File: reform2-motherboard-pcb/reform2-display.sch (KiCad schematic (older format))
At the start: 40 parts, among them J24 EDP_HEADER, U10 SN65DSI86IPAPQ1

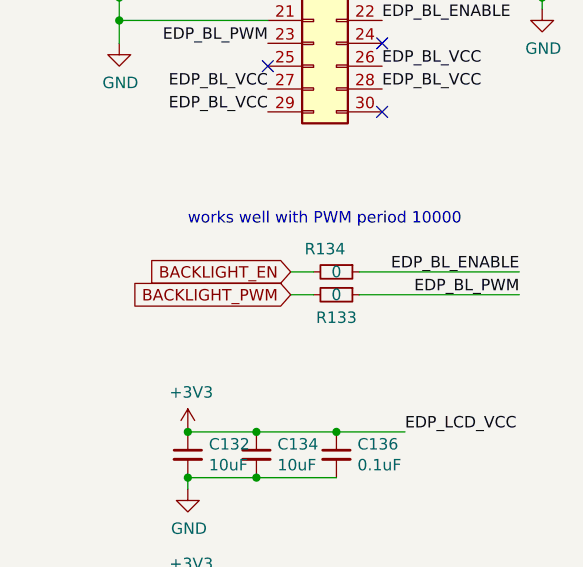
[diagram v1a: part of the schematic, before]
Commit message: reform2-motherboard: version D-4 finished; fixes critical D-3 bugs; adds PCIe refclk termination, speaker output filter stage, pcie0 3v3 load switch, imx reset line to lpc, charge current control line to lpc
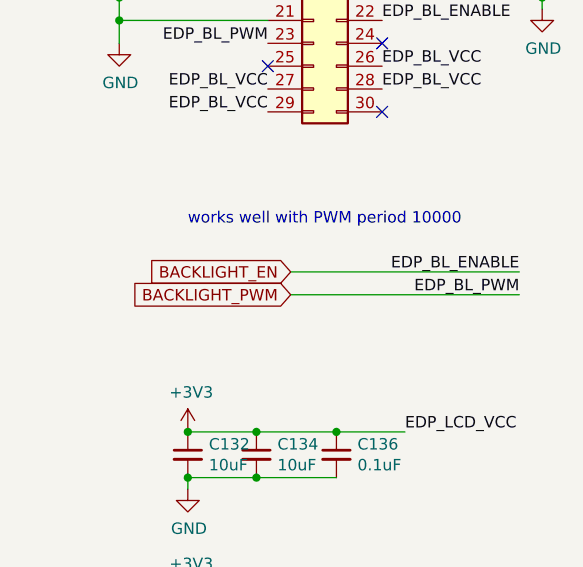
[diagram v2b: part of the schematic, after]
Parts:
- removed R133, R134: 0, Resistor_SMD:R_0603_1608Metric, symbol Device:R_Small
- TP4, TP6, TP7, TP9: DNP (none) -> y
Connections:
- net EDP_BL_ENABLE is gone; now on net BACKLIGHT_EN: J24.22 (Pin_22)
- net EDP_BL_PWM is gone; now on net BACKLIGHT_PWM: J24.23 (Pin_23)
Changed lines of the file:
@@
 Sheet 6 9
 Title "MNT Reform 2 Internal Display"
-Date "2020-04-11"
+Date "2020-05-19"
 Rev "2.0D-4"
 Comp "MNT Research GmbH"
@@
 Wire Wire Line
 	9300 4150 9600 4150
-$Comp
-L Device:R_Small R133
-U 1 1 5EDE1689
-P 9300 3550
-F 0 "R133" V 9400 3550 50  0000 C CNN
-F 1 "0" V 9300 3550 50  0000 C CNN
-F 2 "Resistor_SMD:R_0603_1608Metric" H 9300 3550 50  0001 C CNN
-F 3 "~" H 9300 3550 50  0001 C CNN
-F 4 "Vishay Dale" H 9300 3550 50  0001 C CNN "Manufacturer"
-F 5 "CRCW06030000Z0EAC" H 9300 3550 50  0001 C CNN "Manufacturer_No"
-F 6 "Mouser" H 9300 3550 50  0001 C CNN "Distributor"
-F 7 "y" H 9300 3550 50  0001 C CNN "Checked"
-	1    9300 3550
-	0    1    1    0
-$EndComp
-Wire Wire Line
-	9400 3550 10100 3550
-$Comp
-L Device:R_Small R134
-U 1 1 5EDF03FF
-P 9300 3450
-F 0 "R134" V 9200 3400 50  0000 C CNN
-F 1 "0" V 9300 3450 50  0000 C CNN
-F 2 "Resistor_SMD:R_0603_1608Metric" H 9300 3450 50  0001 C CNN
-F 3 "~" H 9300 3450 50  0001 C CNN
-F 4 "Vishay Dale" H 9300 3450 50  0001 C CNN "Manufacturer"
-F 5 "CRCW06030000Z0EAC" H 9300 3450 50  0001 C CNN "Manufacturer_No"
-F 6 "Mouser" H 9300 3450 50  0001 C CNN "Distributor"
-F 7 "y" H 9300 3450 50  0001 C CNN "Checked"
-	1    9300 3450
-	0    1    1    0
-$EndComp
-Wire Wire Line
-	10100 3450 9400 3450
 Text GLabel 9100 3450 0    50   Input ~ 0
 BACKLIGHT_EN
-Wire Wire Line
-	9100 3450 9200 3450
 Text GLabel 9100 3550 0    50   Input ~ 0
 BACKLIGHT_PWM
-Wire Wire Line
-	9100 3550 9200 3550
 $Comp
 L reform2:SN65DSI86ZQER U10
@@
 F 4 "y" H 2950 4100 50  0001 C CNN "Checked"
 F 5 "None" H 2950 4100 50  0001 C CNN "Distributor"
+F 6 "y" H 2950 4100 50  0001 C CNN "DNP"
 	1    2950 4100
 	1    0    0    -1
@@
 F 4 "y" H 2800 3850 50  0001 C CNN "Checked"
 F 5 "None" H 2800 3850 50  0001 C CNN "Distributor"
+F 6 "y" H 2800 3850 50  0001 C CNN "DNP"
 	1    2800 3850
 	1    0    0    -1
@@
 F 4 "y" H 2650 3650 50  0001 C CNN "Checked"
 F 5 "None" H 2650 3650 50  0001 C CNN "Distributor"
+F 6 "y" H 2650 3650 50  0001 C CNN "DNP"
 	1    2650 3650
 	1    0    0    -1
@@
 F 4 "y" H 2500 3450 50  0001 C CNN "Checked"
 F 5 "None" H 2500 3450 50  0001 C CNN "Distributor"
+F 6 "y" H 2500 3450 50  0001 C CNN "DNP"
 	1    2500 3450
 	1    0    0    -1
@@
 NoConn ~ 9000 2050
 NoConn ~ 9500 1950
+Wire Wire Line
+	9100 3550 10100 3550
+Wire Wire Line
+	9100 3450 10100 3450
 $EndSCHEMATC

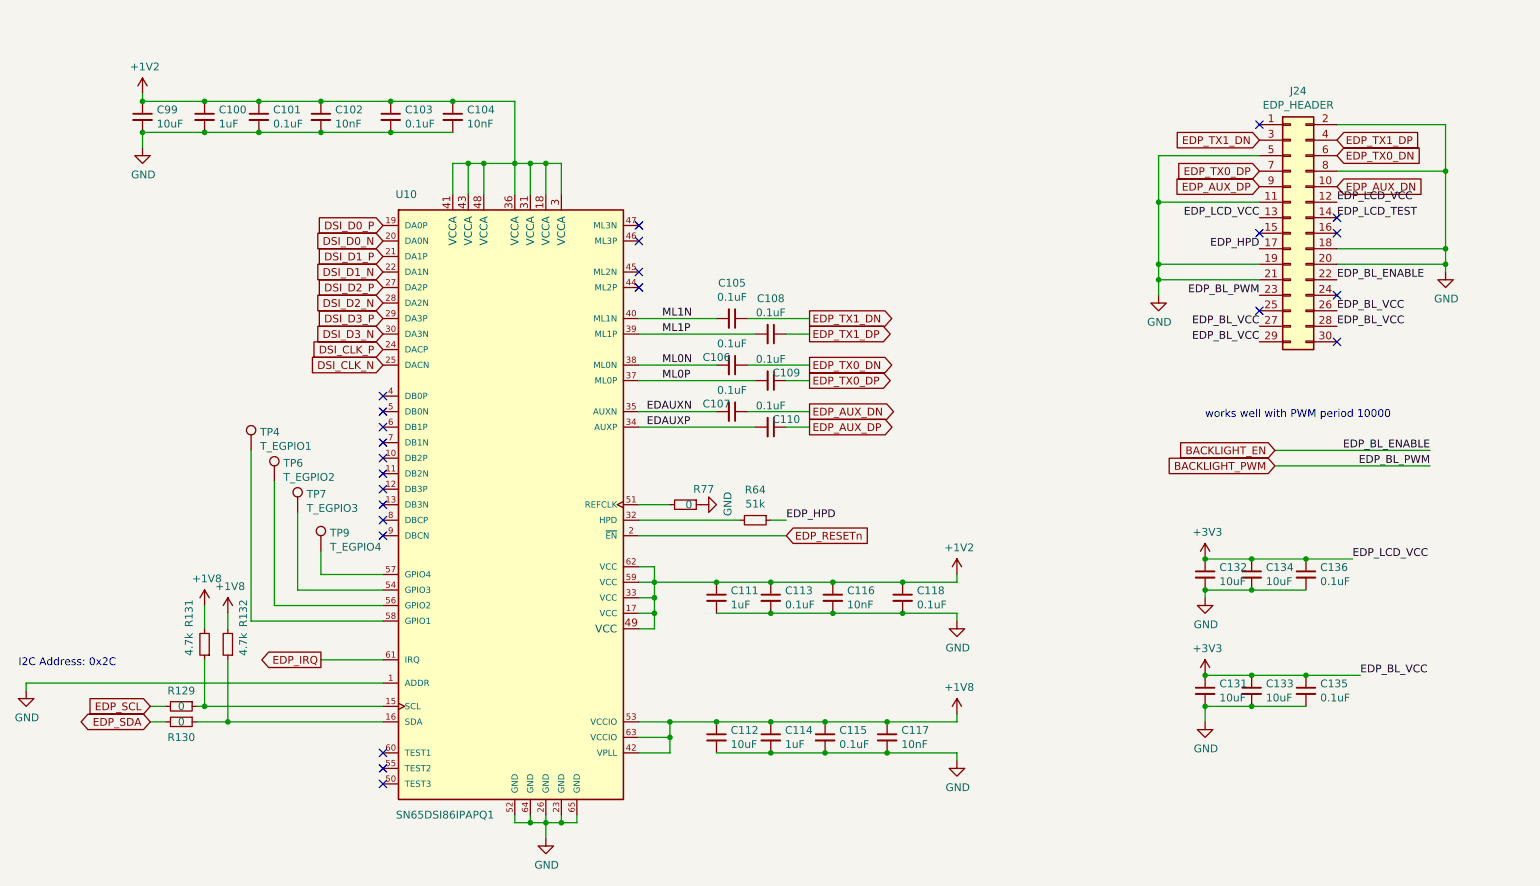
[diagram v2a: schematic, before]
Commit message: reform2-motherboard: first R-1 snapshot. main changes: EMI, ESD, audio filter, enable FETs, SHDN fix, more rail switches
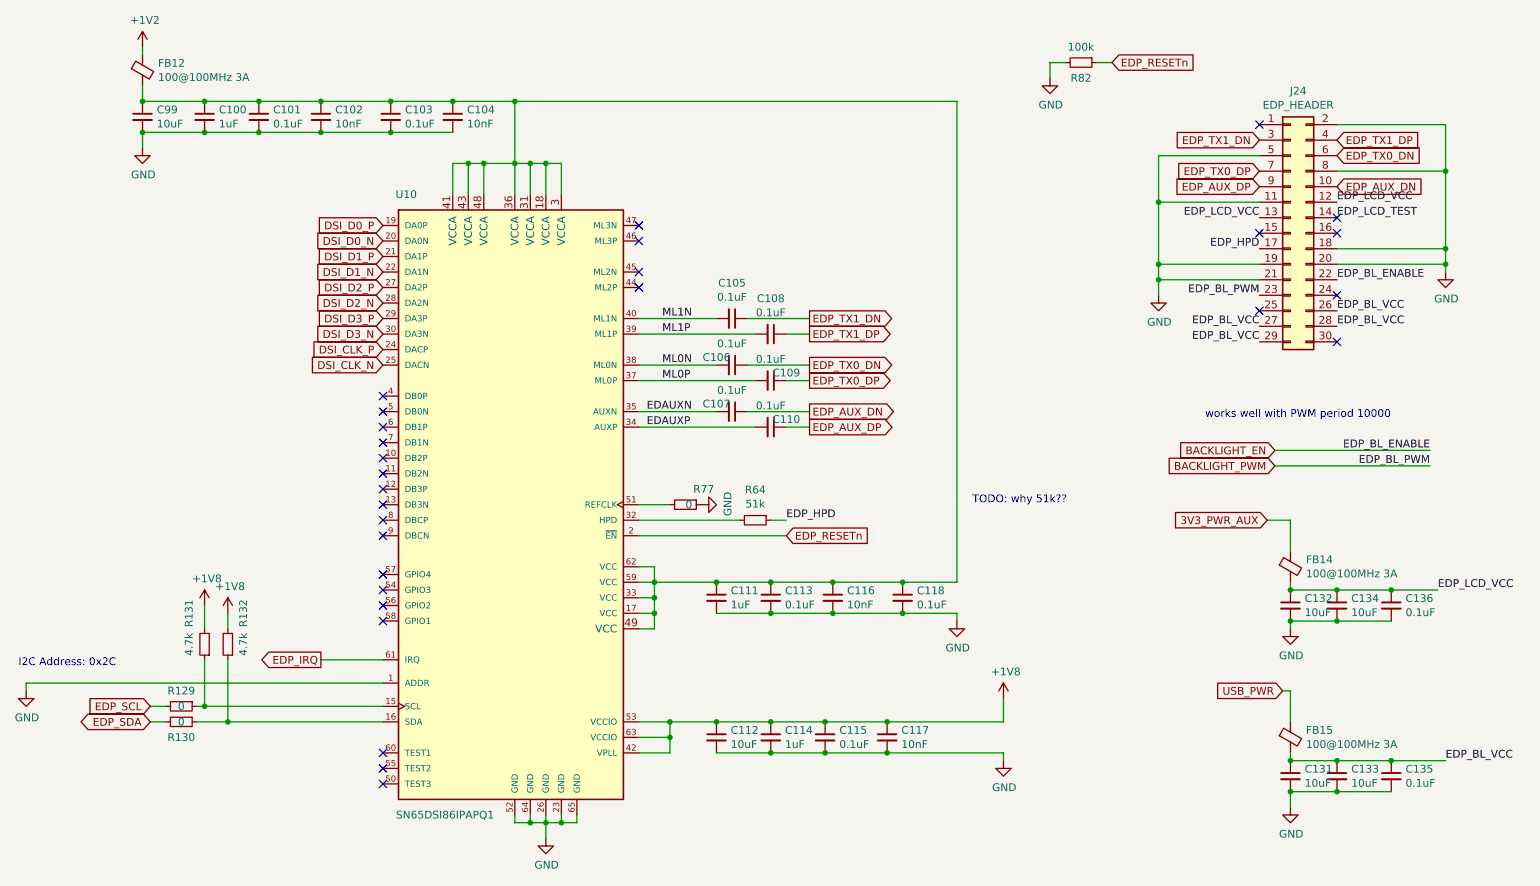
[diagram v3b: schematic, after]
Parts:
- removed TP4: T_EGPIO1, TestPoint:TestPoint_Pad_D1.0mm, symbol Connector:TestPoint
- removed TP6: T_EGPIO2, TestPoint:TestPoint_Pad_D1.0mm, symbol Connector:TestPoint
- removed TP7: T_EGPIO3, TestPoint:TestPoint_Pad_D1.0mm, symbol Connector:TestPoint
- removed TP9: T_EGPIO4, TestPoint:TestPoint_Pad_D1.0mm, symbol Connector:TestPoint
- added FB12, FB14, FB15: 100@100MHz 3A, Inductor_SMD:L_0603_1608Metric, symbol Device:Ferrite_Bead_Small
- added R82: 100k, Resistor_SMD:R_0603_1608Metric, symbol Device:R_Small
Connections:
- net +1V2: now also FB12.1; no longer C100.1, C101.1, C102.1, C103.1, C104.1, C111.1, C113.1, C116.1, C118.1, C99.1, U10.17 (VCC), U10.18 (VCCA), U10.3 (VCCA), U10.31 (VCCA), U10.33 (VCC), U10.36 (VCCA), U10.41 (VCCA), U10.43 (VCCA), U10.48 (VCCA), U10.49 (VCC), U10.59 (VCC), U10.62 (VCC)
- net EDP_RESETn: now also R82.1
- net GND: now also R82.2
- net +3V3 renamed EDP_BL_VCC
- net EDP_BL_VCC: now also FB15.2; no longer C132.1, C134.1, C136.1, J24.12 (Pin_12), J24.13 (Pin_13)
- new net: C100.1, C101.1, C102.1, C103.1, C104.1, C111.1, C113.1, C116.1, C118.1, C99.1, FB12.2, U10.17 (VCC), U10.18 (VCCA), U10.3 (VCCA), U10.31 (VCCA), U10.33 (VCC), U10.36 (VCCA), U10.41 (VCCA), U10.43 (VCCA), U10.48 (VCCA), U10.49 (VCC), U10.59 (VCC), U10.62 (VCC)
- new net 3V3_PWR_AUX: FB14.1
- new net EDP_LCD_VCC: C132.1, C134.1, C136.1, FB14.2, J24.12 (Pin_12), J24.13 (Pin_13)
- new net USB_PWR: FB15.1
- no-connect marks 24 -> 28
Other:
- note added: "TODO: why 51k??"
- moved on the sheet: C131, C132, C133, C134, C135, C136

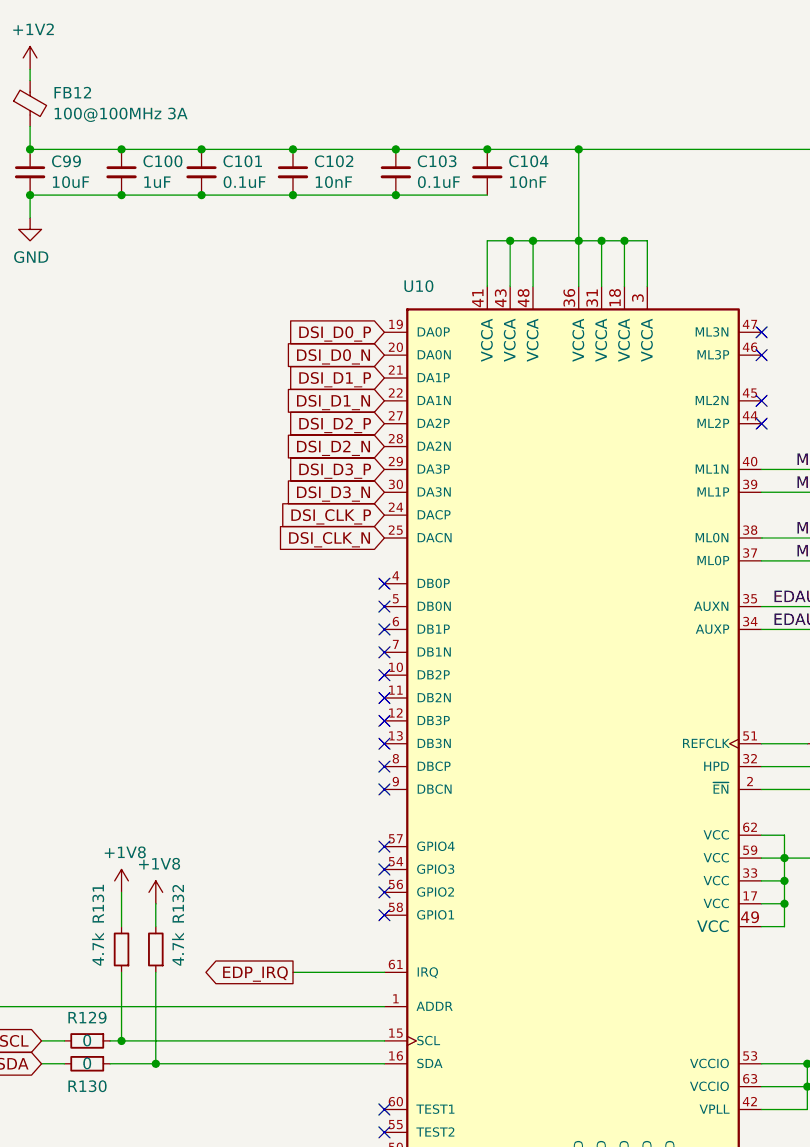
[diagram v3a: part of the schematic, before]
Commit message: reform2-motherboard: R-1 silkscreen cleanup; usb hub reset pulldown added
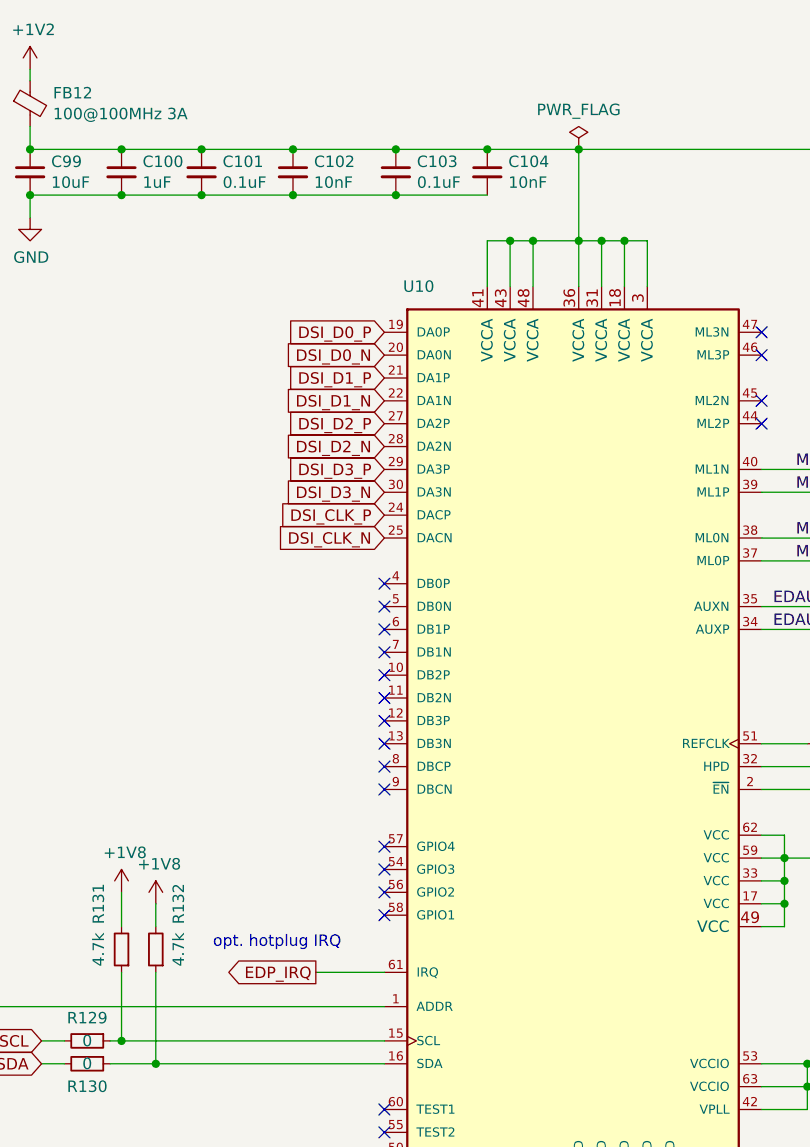
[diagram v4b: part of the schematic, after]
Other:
- note added: "opt. hotplug IRQ"
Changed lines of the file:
@@
 $EndComp
-Wire Wire Line
-	3800 1600 3900 1600
 Wire Wire Line
 	4500 1600 4500 1800
 Wire Wire Line
 	3800 1600 3800 1800
-Wire Wire Line
-	3900 1800 3900 1600
-Connection ~ 3900 1600
-Wire Wire Line
-	3900 1600 4000 1600
 Wire Wire Line
 	4000 1600 4000 1800
@@
 Text GLabel 5950 4000 2    50   Input ~ 0
 EDP_RESETn
-Text GLabel 2950 4800 0    50   Output ~ 0
+Text GLabel 3050 4800 0    50   Output ~ 0
 EDP_IRQ
 NoConn ~ 5000 2000
@@
 EDP_SCL
 Wire Wire Line
-	2950 4800 3350 4800
+	3050 4800 3350 4800
 Wire Wire Line
 	4000 1600 4200 1600
@@
 Wire Wire Line
 	9200 3900 9200 4100
+Wire Wire Line
+	3800 1600 3900 1600
+Wire Wire Line
+	3900 1800 3900 1600
+Connection ~ 3900 1600
+Wire Wire Line
+	3900 1600 4000 1600
+$Comp
+L power:PWR_FLAG #FLG0123
+U 1 1 64C4E0F7
+P 4200 1200
+F 0 "#FLG0123" H 4200 1275 50  0001 C CNN
+F 1 "PWR_FLAG" H 4200 1373 50  0000 C CNN
+F 2 "" H 4200 1200 50  0001 C CNN
+F 3 "~" H 4200 1200 50  0001 C CNN
+	1    4200 1200
+	1    0    0    -1
+$EndComp
+Text Notes 2600 4700 0    50   ~ 0
+opt. hotplug IRQ
 $EndSCHEMATC

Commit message: motherboard: r-1 release snapshot
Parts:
- C100, C111, C114: Manufacturer_No UMK107AB7105KA-T -> UMK107BJ105KA-T
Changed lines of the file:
@@
 Sheet 6 9
 Title "MNT Reform 2 Internal Display"
-Date "2020-05-19"
-Rev "2.0D-4"
+Date "2020-09-24"
+Rev "2.0R-1"
 Comp "MNT Research GmbH"
 Comment1 "https://mntre.com"
@@
 F 3 "~" H 2200 1300 50  0001 C CNN
 F 4 "Taiyo Yuden" H 2200 1300 50  0001 C CNN "Manufacturer"
-F 5 "UMK107AB7105KA-T" H 2200 1300 50  0001 C CNN "Manufacturer_No"
+F 5 "UMK107BJ105KA-T" H 2200 1300 50  0001 C CNN "Manufacturer_No"
 F 6 "y" H 2200 1300 50  0001 C CNN "Checked"
 F 7 "Mouser" H 2200 1300 50  0001 C CNN "Distributor"
@@
 F 3 "~" H 5500 4400 50  0001 C CNN
 F 4 "Taiyo Yuden" H 5500 4400 50  0001 C CNN "Manufacturer"
-F 5 "UMK107AB7105KA-T" H 5500 4400 50  0001 C CNN "Manufacturer_No"
+F 5 "UMK107BJ105KA-T" H 5500 4400 50  0001 C CNN "Manufacturer_No"
 F 6 "y" H 5500 4400 50  0001 C CNN "Checked"
 F 7 "Mouser" H 5500 4400 50  0001 C CNN "Distributor"
@@
 F 3 "~" H 5850 5300 50  0001 C CNN
 F 4 "Taiyo Yuden" H 5850 5300 50  0001 C CNN "Manufacturer"
-F 5 "UMK107AB7105KA-T" H 5850 5300 50  0001 C CNN "Manufacturer_No"
+F 5 "UMK107BJ105KA-T" H 5850 5300 50  0001 C CNN "Manufacturer_No"
 F 6 "y" H 5850 5300 50  0001 C CNN "Checked"
 F 7 "Mouser" H 5850 5300 50  0001 C CNN "Distributor"

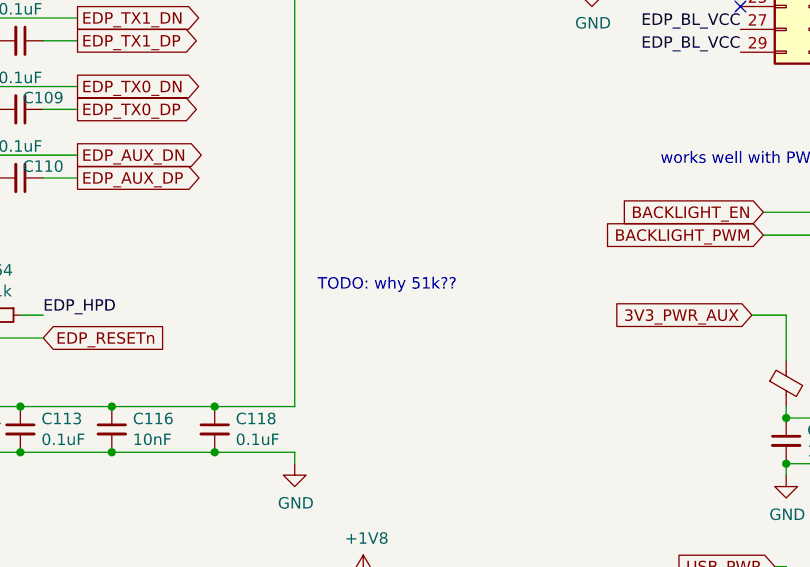
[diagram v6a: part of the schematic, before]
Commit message: reform2-motherboard: add pdf schematics
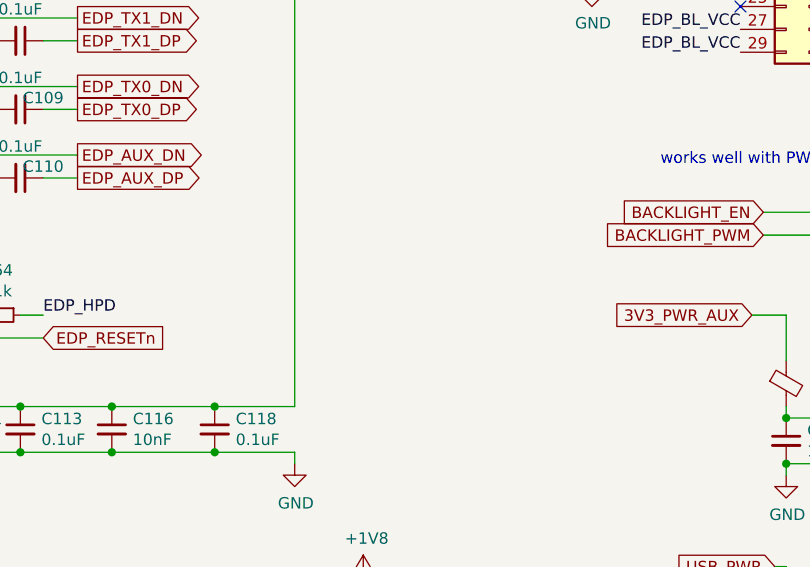
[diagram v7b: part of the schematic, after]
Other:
- note removed: "TODO: why 51k??"
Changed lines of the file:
@@
 NoConn ~ 3350 4450
 NoConn ~ 3350 4550
-Text Notes 7150 3800 0    50   ~ 0
-TODO: why 51k??
 Text GLabel 9050 3900 0    50   Input ~ 0
 3V3_PWR_AUX
